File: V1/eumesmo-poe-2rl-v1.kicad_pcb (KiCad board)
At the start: 4 copper layers, 82.5 x 45 mm, 105 parts, among them J1 USB_C_Receptacle_USB2.0, J2 250-202, J3 RJ45 JACK, J4 250-202, K1 G5NB-1A-E-DC5, K2 G5NB-1A-E-DC5, Q1 UMH3N, Q2 MMBT2222A, Q3 WPM2015-3/TR, Q4 LMUN2211LT1G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

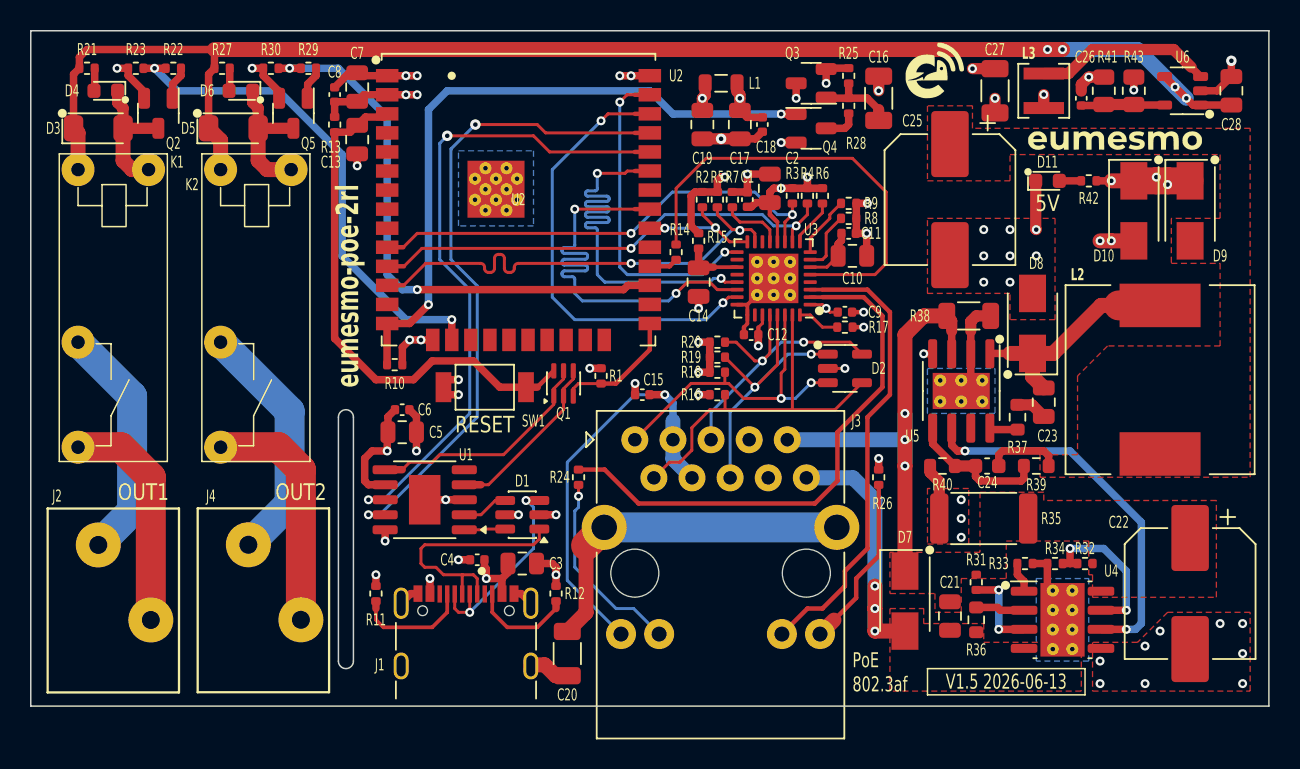
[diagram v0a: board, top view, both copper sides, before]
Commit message: Rerouted ETH TX/RX pairs.
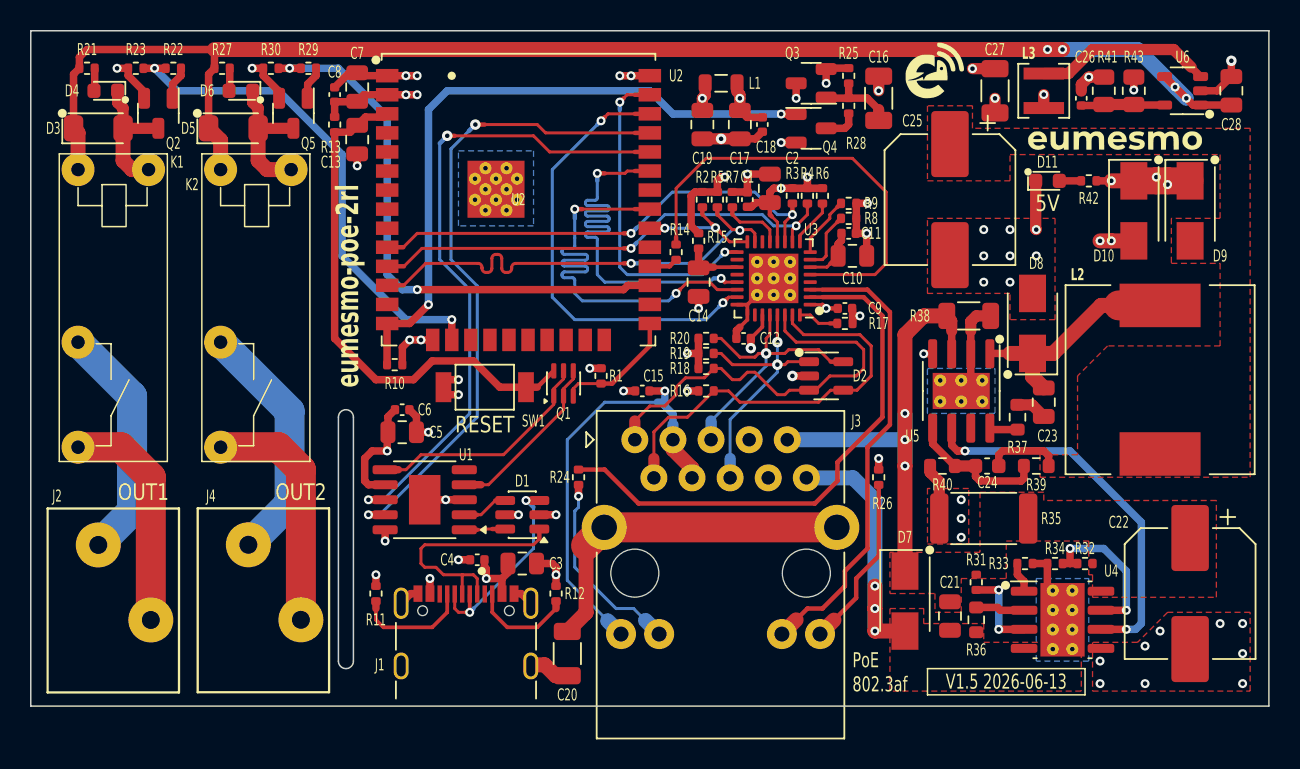
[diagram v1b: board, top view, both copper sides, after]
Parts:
- moved D2 1.35 mm to (129.0, 94.0)
- moved R16 0.79 mm to (121.0, 95.0)
- moved R18 0.79 mm to (121.0, 93.5)
- moved R19 0.79 mm to (121.0, 92.5)
- moved R20 0.79 mm to (121.0, 91.5)
- moved C12 0.56 mm to (123.5, 91.5)
- moved C15 0.25 mm to (116.8, 95.0)
- moved C9 0.25 mm to (130.2, 89.5)
- moved R17 0.25 mm to (130.2, 90.5)
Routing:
- net /ETHRXD-: track 21.7 -> 27.7 mm, vias 2 -> 0
- net /ETHRXD+: track 24.7 -> 28.1 mm
- net /ETHTXD+: track 20.7 -> 18.9 mm
- net +3V3A: track 48.6 -> 47.1 mm, vias 7 -> 6
- net /ETHTXD-: track 20.4 -> 19.6 mm, vias 2 -> 1
- net /ETHLEDYK: track 13.8 -> 13.1 mm
- net GND: track 71.6 -> 71.3 mm, vias 52 -> 51
